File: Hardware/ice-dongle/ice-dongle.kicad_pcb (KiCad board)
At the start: 4 copper layers, 40 x 16 mm, 48 parts, among them J1 USB_C_Receptacle_USB2.0, J2 NC Jumper, J3 PROG HEADER, J4 FFC2B35-18-G_REVA2, J5 Qwiic, SW1 SW_Push, SW2 SW_Push, U1 APS6404L-3SQR, U2 W25Q64JWUUIQ, U3 DRTR5V0U4S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

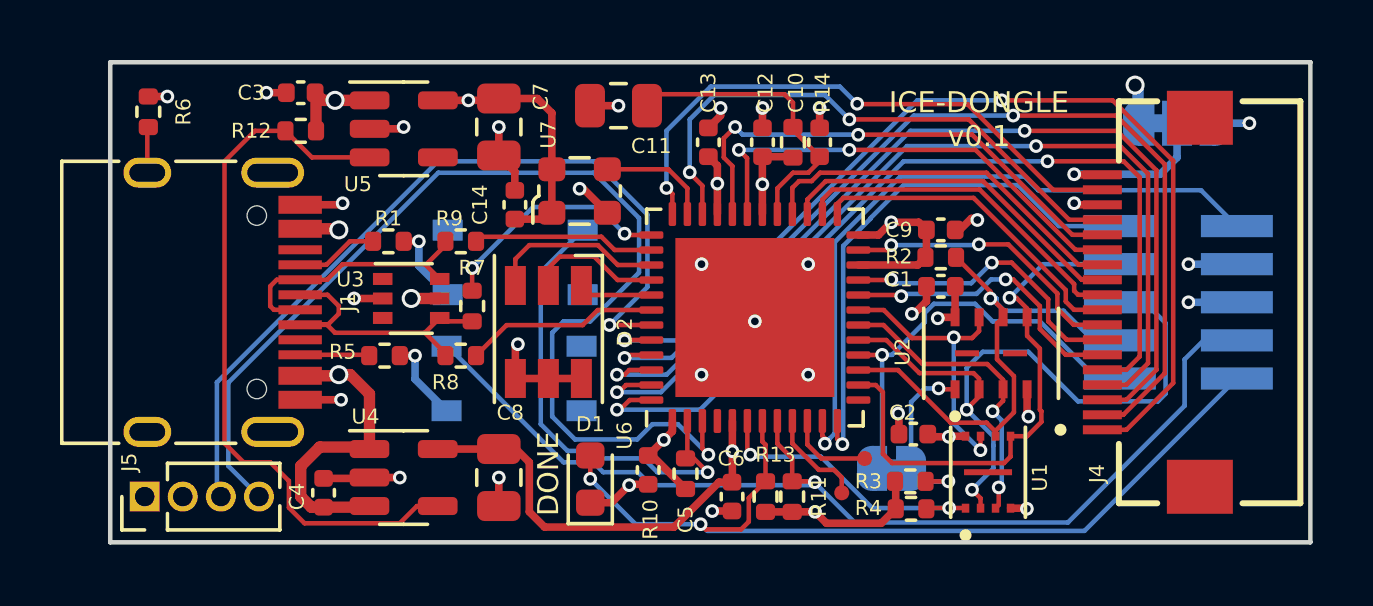
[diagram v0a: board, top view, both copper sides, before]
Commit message: Corrected swapped silkscreen refdes, bumped version to 0.1a
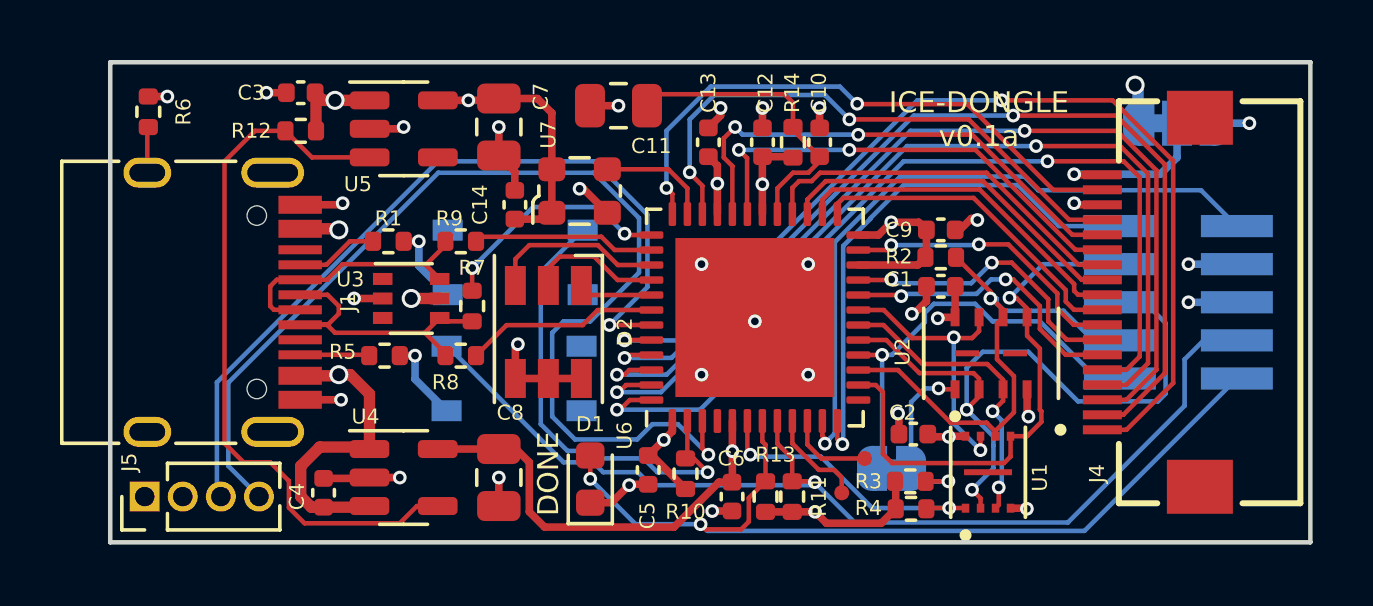
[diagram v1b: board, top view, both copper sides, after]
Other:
- board text added: "ICE-DONGLE v0.1a"
- board text removed: "ICE-DONGLE v0.1"
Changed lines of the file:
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@@
     (property "Sheetname" "")
     (attr smd)
-    (fp_text reference "R10" (at -1.526 -1.17 90) (layer "F.SilkS")
+    (fp_text reference "R10" (at -1.272 0 180) (layer "F.SilkS")
       (effects (font (size 0.5 0.5) (thickness 0.075)))
     )
@@
     (property "Sheetname" "")
     (attr smd)
-    (fp_text reference "C10" (at 1.651 -0.7874 90) (layer "F.SilkS")
+    (fp_text reference "C10" (at 1.651 -0.0254 90) (layer "F.SilkS")
       (effects (font (size 0.5 0.5) (thickness 0.075)))
     )
@@
     (property "Sheetname" "")
     (attr smd)
-    (fp_text reference "R14" (at -1.651 -0.9906 90) (layer "F.SilkS")
+    (fp_text reference "R14" (at -1.651 0.0254 90) (layer "F.SilkS")
       (effects (font (size 0.5 0.5) (thickness 0.075)))
     )
@@
     (property "Sheetname" "")
     (attr smd)
-    (fp_text reference "C5" (at 1.651 -1.2446 90) (layer "F.SilkS")
+    (fp_text reference "C5" (at 1.524 0.0254 90) (layer "F.SilkS")
       (effects (font (size 0.5 0.5) (thickness 0.075)))
     )
@@
     (effects (font (size 0.5 0.5) (thickness 0.07)) (justify mirror))
   )
-  (gr_text "ICE-DONGLE\nv0.1" (at 130.556 103.505) (layer "F.SilkS")
+  (gr_text "ICE-DONGLE\nv0.1a" (at 130.556 103.505) (layer "F.SilkS")
     (effects (font (size 0.7 0.7) (thickness 0.1)))
   )
